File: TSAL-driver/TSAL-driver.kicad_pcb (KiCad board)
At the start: 2 copper layers, 28 parts, among them J1 OUT+, J2 OUT-, J3 IN+, J4 IN-, Q1 Q_PMOS_DGS, Q2 Q_NMOS_DGS, Q3 Q_NMOS_DGS, Q4 Q_NMOS_DGS, U1 LM556

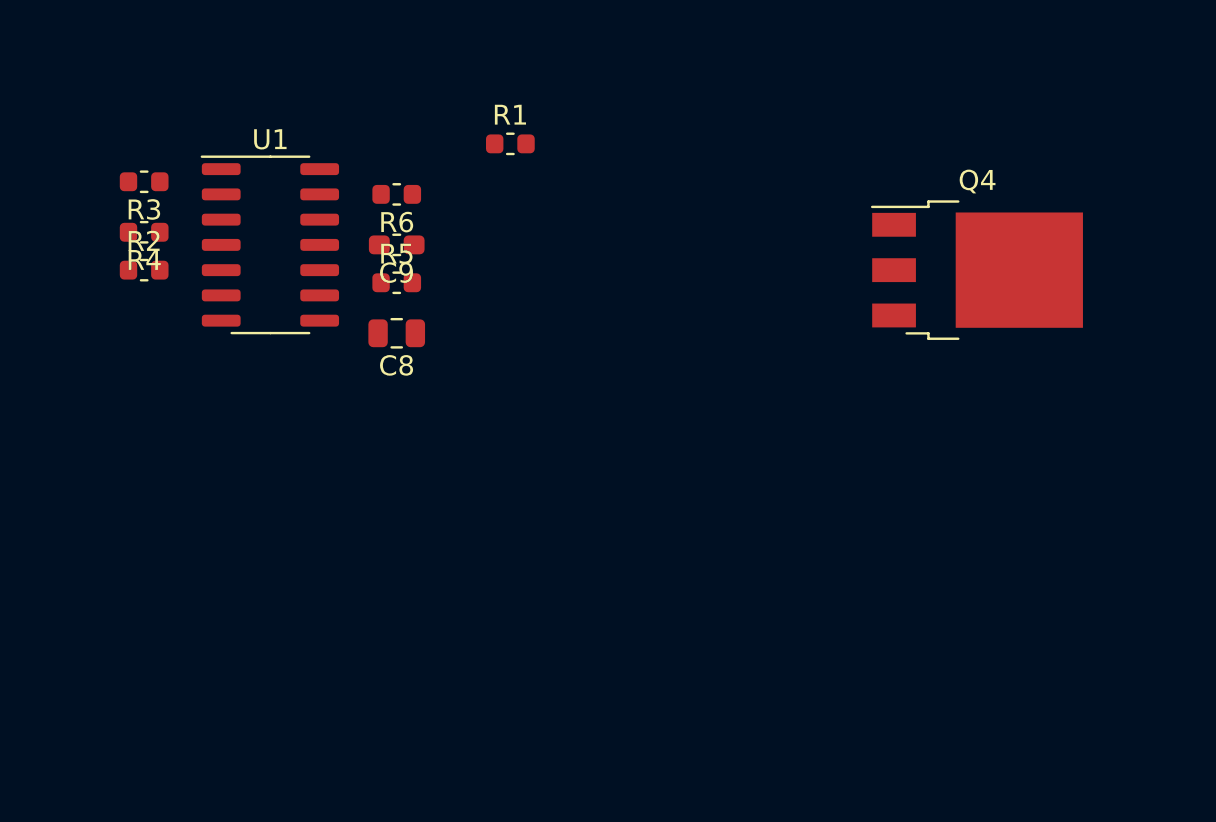
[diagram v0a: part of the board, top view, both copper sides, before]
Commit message: Started laying out TSAL-driver
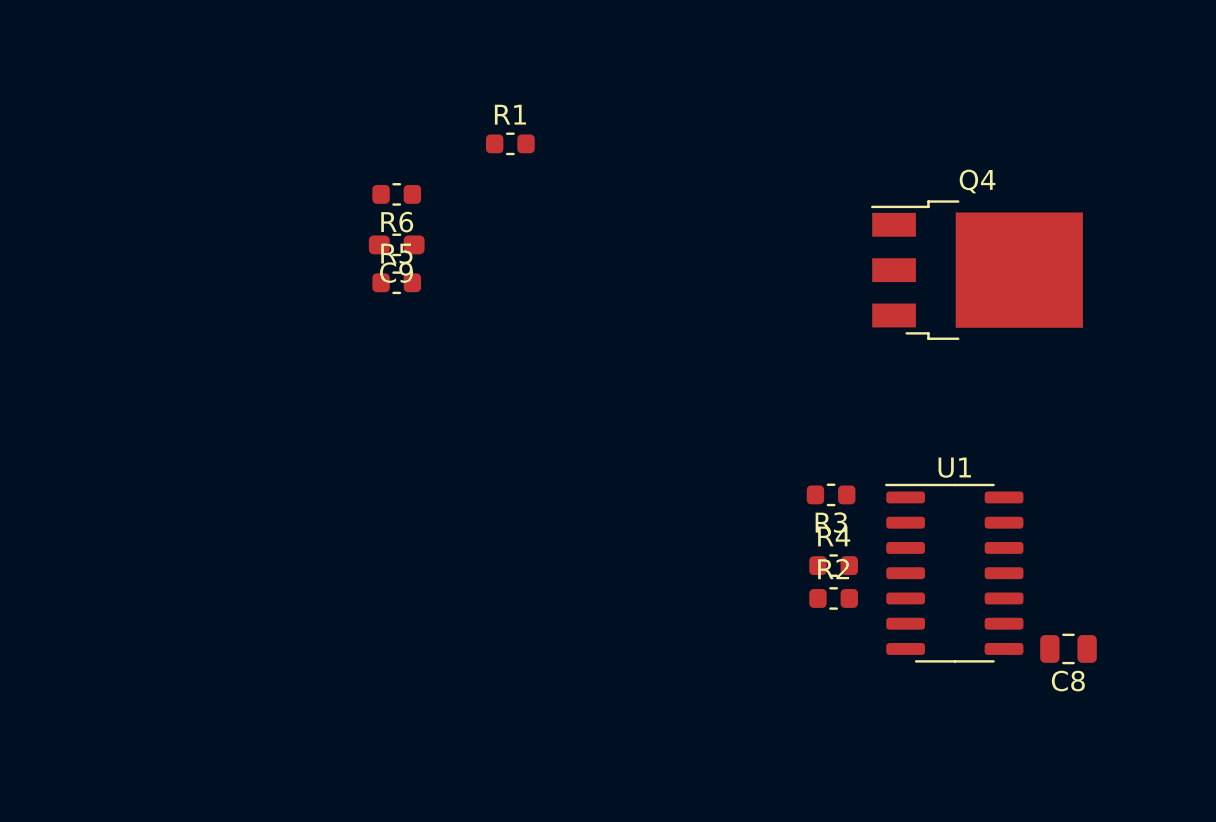
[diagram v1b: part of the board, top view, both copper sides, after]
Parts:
- moved R4 38.5 mm to (139.4, 111.4), turned to 0 degrees
- moved R2 38.4 mm to (139.4, 113.0)
- moved U1 38.2 mm to (145.5, 111.8)
- moved R3 38.0 mm to (139.3, 107.8)
- moved C8 37.3 mm to (151.3, 115.6)
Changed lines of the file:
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@@
-(kicad_pcb (version 20171130) (host pcbnew 5.1.4-e60b266~84~ubuntu16.04.1)
+(kicad_pcb (version 20171130) (host pcbnew "(5.1.2)-2")
   (general
     (thickness 1.6)
@@
     (solder_mask_min_width 0.25)
     (aux_axis_origin 0 0)
-    (visible_elements FFFFFF7F)
+    (visible_elements 7FFFFFFF)
     (pcbplotparams
       (layerselection 0x010fc_ffffffff)
@@
   )
   (module Capacitor_SMD:C_0805_2012Metric (layer F.Cu)
-    (at 117.475 99.695 180)
+    (at 151.257 115.57 180)
     (descr "Capacitor SMD 0805 (2012 Metric), square (rectangular) end terminal, IPC_7351 nominal, (Body size source: https://docs.google.com/spreadsheets/d/1BsfQQcO9C6DZCsRaXUlFlo91Tg2WpOkGARC1WS5S8t0/edit?usp=sharing), generated with kicad-footprint-generator")
     (tags capacitor)
@@
   )
   (module Resistor_SMD:R_0603_1608Metric (layer F.Cu)
-    (at 104.775 96.52)
+    (at 139.446 113.03)
     (descr "Resistor SMD 0603 (1608 Metric), square (rectangular) end terminal, IPC_7351 nominal, (Body size source: http://www.tortai-tech.com/upload/download/2011102023233369053.pdf), generated with kicad-footprint-generator")
     (tags resistor)
@@
   )
   (module Resistor_SMD:R_0603_1608Metric (layer F.Cu)
-    (at 104.775 92.075 180)
+    (at 139.319 107.823 180)
     (descr "Resistor SMD 0603 (1608 Metric), square (rectangular) end terminal, IPC_7351 nominal, (Body size source: http://www.tortai-tech.com/upload/download/2011102023233369053.pdf), generated with kicad-footprint-generator")
     (tags resistor)
@@
   )
   (module Resistor_SMD:R_0603_1608Metric (layer F.Cu)
-    (at 104.775 94.615 180)
+    (at 139.446 111.379)
     (descr "Resistor SMD 0603 (1608 Metric), square (rectangular) end terminal, IPC_7351 nominal, (Body size source: http://www.tortai-tech.com/upload/download/2011102023233369053.pdf), generated with kicad-footprint-generator")
     (tags resistor)
@@
       (effects (font (size 0.4 0.4) (thickness 0.06)))
     )
-    (pad 1 smd roundrect (at -0.7875 0 180) (size 0.875 0.95) (layers F.Cu F.Paste F.Mask) (roundrect_rratio 0.25)
+    (pad 1 smd roundrect (at -0.7875 0) (size 0.875 0.95) (layers F.Cu F.Paste F.Mask) (roundrect_rratio 0.25)
       (net 1 +12V))
-    (pad 2 smd roundrect (at 0.7875 0 180) (size 0.875 0.95) (layers F.Cu F.Paste F.Mask) (roundrect_rratio 0.25)
+    (pad 2 smd roundrect (at 0.7875 0) (size 0.875 0.95) (layers F.Cu F.Paste F.Mask) (roundrect_rratio 0.25)
       (net 3 "Net-(C2-Pad2)"))
     (model ${KISYS3DMOD}/Resistor_SMD.3dshapes/R_0603_1608Metric.wrl
@@
   )
   (module Package_SO:SOIC-14_3.9x8.7mm_P1.27mm (layer F.Cu)
-    (at 111.125 95.25)
+    (at 145.542 111.76)
     (descr "SOIC, 14 Pin (JEDEC MS-012AB, https://www.analog.com/media/en/package-pcb-resources/package/pkg_pdf/soic_narrow-r/r_14.pdf), generated with kicad-footprint-generator ipc_gullwing_generator.py")
     (tags "SOIC SO")

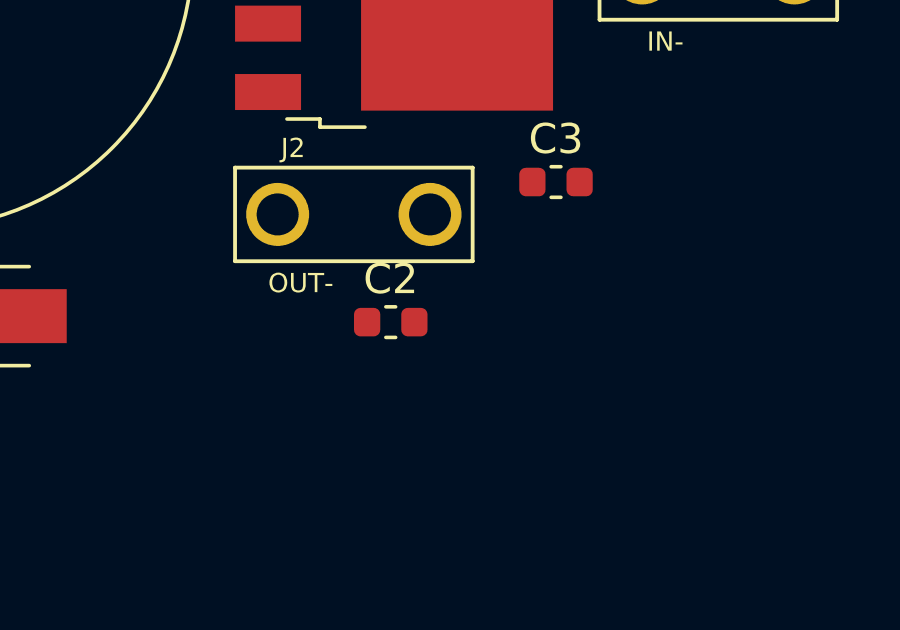
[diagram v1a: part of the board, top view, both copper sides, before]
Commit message: Moved capictor
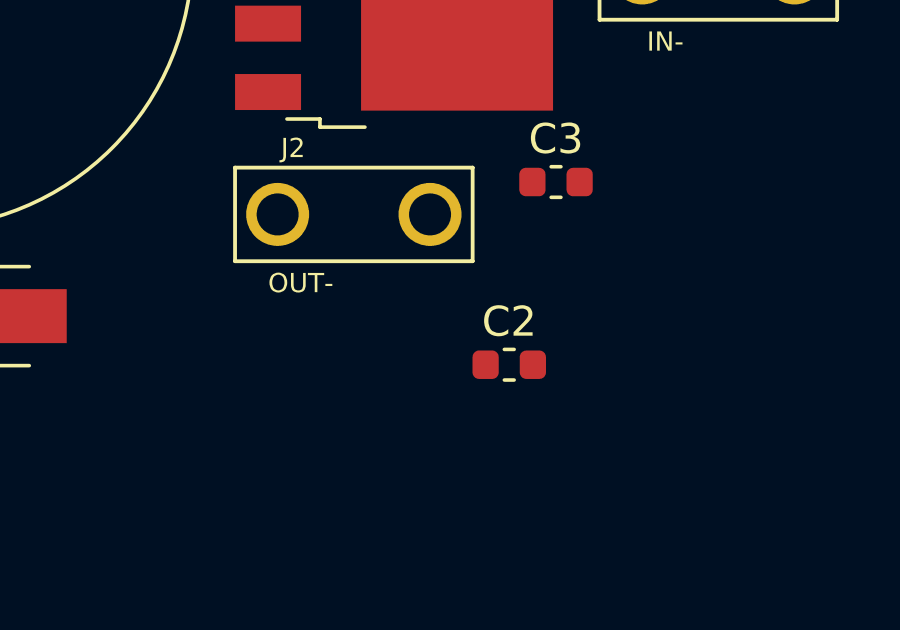
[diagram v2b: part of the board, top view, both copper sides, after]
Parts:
- moved C2 4.20 mm to (145.4, 74.3)
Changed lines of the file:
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@@
-(kicad_pcb (version 20171130) (host pcbnew "(5.1.2)-2")
+(kicad_pcb (version 20171130) (host pcbnew "(5.0.1)-3")
   (general
     (thickness 1.6)
@@
     (zone_45_only no)
     (trace_min 0.2)
+    (segment_width 0.2)
+    (edge_width 0.05)
     (via_size 0.8)
     (via_drill 0.4)
@@
     (uvia_min_size 0.2)
     (uvia_min_drill 0.1)
-    (edge_width 0.05)
-    (segment_width 0.2)
     (pcb_text_width 0.3)
     (pcb_text_size 1.5 1.5)
@@
   )
   (module Capacitor_SMD:C_0603_1608Metric (layer F.Cu)
-    (at 141.465001 72.875001)
+    (at 145.415 74.295)
     (descr "Capacitor SMD 0603 (1608 Metric), square (rectangular) end terminal, IPC_7351 nominal, (Body size source: http://www.tortai-tech.com/upload/download/2011102023233369053.pdf), generated with kicad-footprint-generator")
     (tags capacitor)

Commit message: Organized TSAL-Driver board
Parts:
- moved R7 73.3 mm to (133.0, 115.0)
- moved J1 67.9 mm to (134.0, 93.5), turned to 270 degrees
- moved Q1 67.5 mm to (123.1, 115.0), turned to 180 degrees
- moved C5 65.7 mm to (158.2, 104.5), turned to 180 degrees
- moved J3 64.8 mm to (140.0, 94.0), turned to 270 degrees
- moved C7 58.3 mm to (107.0, 117.0), turned to 90 degrees
- moved C4 57.2 mm to (153.5, 104.5), turned to 180 degrees
- moved D1 56.7 mm to (156.0, 116.0)
- moved Q3 47.9 mm to (123.0, 99.0), turned to 180 degrees
- moved Q2 47.8 mm to (123.0, 107.0), turned to 180 degrees
- moved D2 47.8 mm to (156.0, 111.0), turned to 180 degrees
- moved C3 46.8 mm to (147.8, 115.0)
- moved C1 38.3 mm to (161.0, 93.0), turned to 180 degrees
- moved C2 36.8 mm to (147.8, 111.0), turned to 180 degrees
- moved C6 34.7 mm to (107.0, 95.0), turned to 90 degrees
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
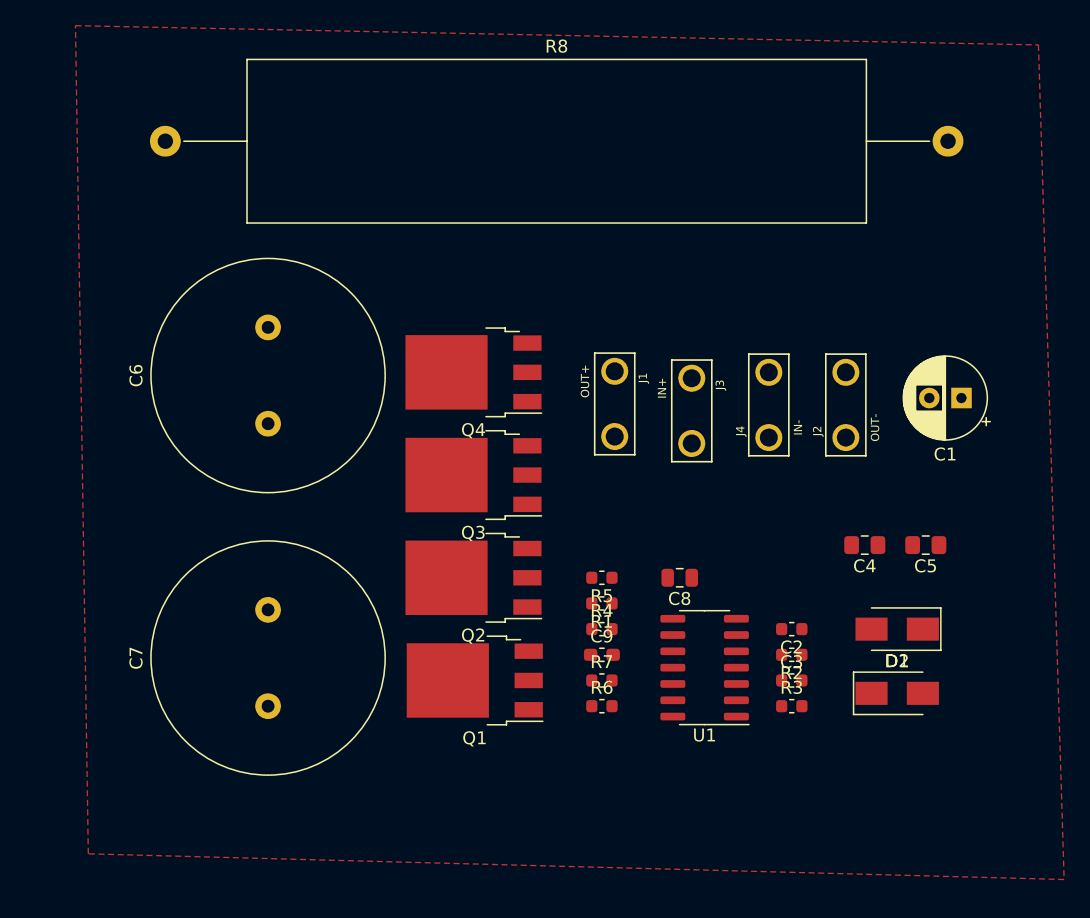
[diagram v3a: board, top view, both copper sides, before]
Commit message: Inputs and Outputs are on Opposite Sides
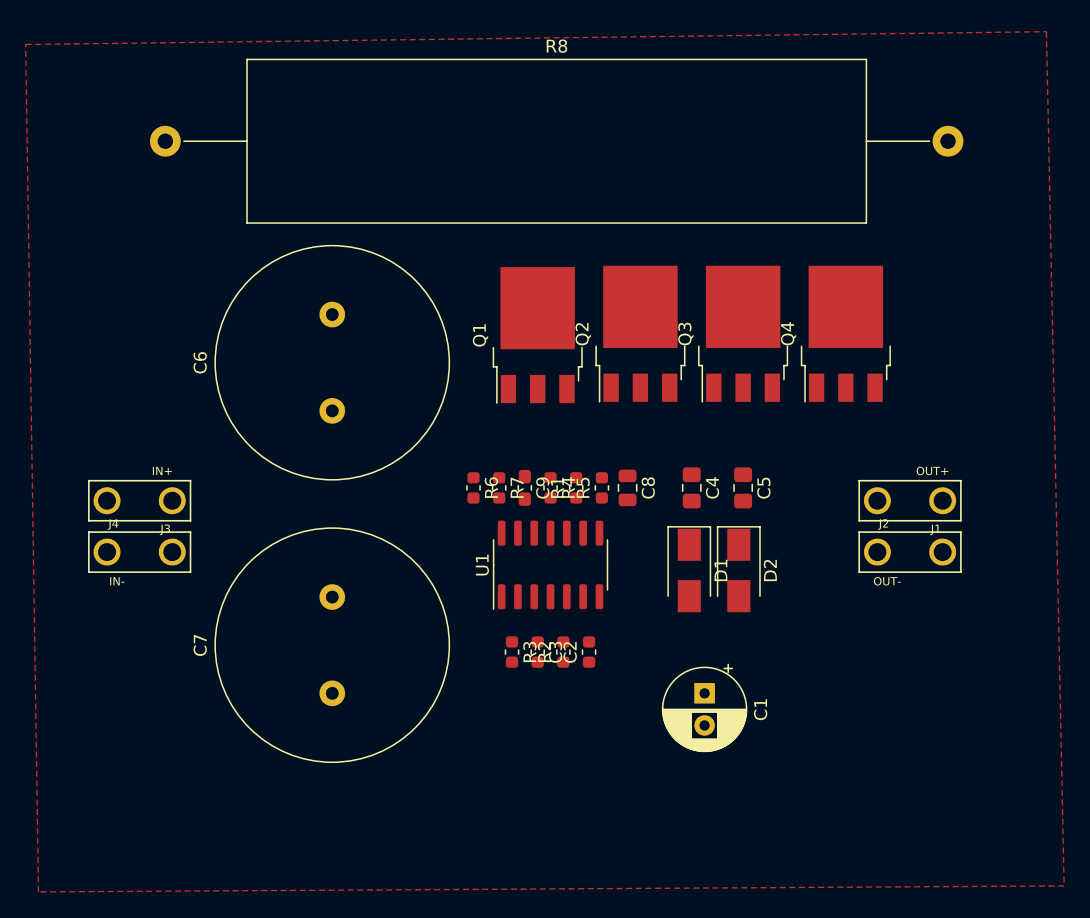
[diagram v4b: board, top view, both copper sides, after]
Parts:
- moved J4 50.3 mm to (97.0, 105.0), turned to 0 degrees
- moved J3 43.6 mm to (97.0, 101.0), turned to 180 degrees
- moved C1 30.5 mm to (141.0, 116.0), turned to 270 degrees
- moved Q4 29.2 mm to (152.0, 88.0), turned to 90 degrees
- moved Q1 27.3 mm to (128.0, 88.1), turned to 90 degrees
- moved J1 24.2 mm to (157.0, 101.0), turned to 180 degrees
- moved Q3 23.7 mm to (144.0, 88.0), turned to 90 degrees
- moved Q2 23.0 mm to (136.0, 88.0), turned to 90 degrees
- moved R3 22.2 mm to (126.0, 112.8), turned to 270 degrees
- moved C3 19.9 mm to (128.0, 112.8), turned to 270 degrees
- moved R6 19.7 mm to (123.0, 100.0), turned to 270 degrees
- moved D1 18.8 mm to (139.8, 106.4), turned to 270 degrees
- moved R2 17.8 mm to (130.0, 112.8), turned to 90 degrees
- moved R7 17.0 mm to (125.0, 100.0), turned to 270 degrees
- moved C2 15.9 mm to (132.0, 112.8), turned to 90 degrees
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
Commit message: Finished TSAL-driver
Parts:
- removed C5: 10u, Capacitor_SMD:C_0805_2012Metric_Pad1.15x1.40mm_HandSolder
- removed C6, C7: 4700uF, Capacitor_THT:C_Radial_D18.0mm_H35.5mm_P7.50mm
- removed C8: 10u, Capacitor_SMD:C_0805_2012Metric
- removed C9: 0.01, Capacitor_SMD:C_0603_1608Metric_Pad1.05x0.95mm_HandSolder
- removed D1, D2: 1N4001, Diode_SMD:D_SMA
- removed Q1: Q_PMOS_DGS, Package_TO_SOT_SMD:TO-252-3_TabPin2
- removed Q2, Q3, Q4: Q_NMOS_DGS, Package_TO_SOT_SMD:TO-252-3_TabPin2
- removed R1, R3: 10k, Resistor_SMD:R_0603_1608Metric
- removed R2, R4, R5: 100, Resistor_SMD:R_0603_1608Metric
- removed R6: 4.7k, Resistor_SMD:R_0603_1608Metric
- removed R7: 39k, Resistor_SMD:R_0603_1608Metric
- removed R8: 10, Resistor_THT:R_Axial_Power_L48.0mm_W12.5mm_P60.96mm
- added G***: LOGO, AERO-footprints:AERO_Logo_15x6mm, F.Cu at (130.8, 74.9)
- added U2: ATtiny25-20SSU, Package_SO:SOIC-8_3.9x4.9mm_P1.27mm, F.Cu at (134.0, 87.0)
- added U3: LDB-350L, AERO-footprints:DIP1549W45P254L3404H940Q24, B.Cu at (133.9, 85.9)
- C1: value 100u -> 0.1uF; footprint Capacitor_THT:CP_Radial_D6.3mm_P2.50mm -> Capacitor_SMD:C_0603_1608Metric
- C2: value 10n -> 10uF
- C3: value 0.01u -> 10uF
- C4: value 10u -> 10uF; footprint Capacitor_SMD:C_0805_2012Metric_Pad1.15x1.40mm_HandSolder -> Capacitor_SMD:C_0603_1608Metric
- J1: value OUT+ -> LED+; footprint 1217861-1:TE_1217861-1 -> AERO-footprints:TE_1217861-1
- J2: value OUT- -> LED-; footprint 1217861-1:TE_1217861-1 -> AERO-footprints:TE_1217861-1
- J3: value IN+ -> 12V; footprint 1217861-1:TE_1217861-1 -> AERO-footprints:TE_1217861-1
- J4: value IN- -> GND; footprint 1217861-1:TE_1217861-1 -> AERO-footprints:TE_1217861-1
- U1: value LM556 -> AZ1117-5.0; footprint Package_SO:SOIC-14_3.9x8.7mm_P1.27mm -> Package_TO_SOT_SMD:SOT-223-3_TabPin2
- moved J2 51.4 mm to (127.6, 62.9), turned to 90 degrees
- moved J3 43.5 mm to (139.7, 109.2), turned to 90 degrees
- moved J1 41.9 mm to (139.7, 62.9), turned to 90 degrees
- moved C1 33.2 mm to (135.9, 83.2), turned to 180 degrees
- moved J4 30.9 mm to (127.6, 109.2), turned to 90 degrees
- moved C3 17.6 mm to (129.5, 95.2)
- moved U1 11.4 mm to (135.3, 96.5), turned to 0 degrees
- moved C2 11.2 mm to (132.7, 101.6), turned to 180 degrees
- moved C4 2.24 mm to (138.4, 101.6), turned to 0 degrees
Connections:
- C1 pad 1: +12V -> +5V
- C2 pad 2: Net-(C2-Pad2) -> +12V
- C3 pad 2: Net-(C3-Pad2) -> +5V
- C4 pad 1: Net-(C4-Pad1) -> GND
- C4 pad 2: Net-(C4-Pad2) -> +12V
- J1 pad 1: Net-(J1-Pad1) -> +24V
- J2 pad 1: /LED- -> GND
- U1 pad 1: Net-(R3-Pad1) -> GND
- U1 pad 2: Net-(C2-Pad2) -> +5V
- U1 pad 3: Net-(C3-Pad2) -> +12V
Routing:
- net +12V: track 0.00 -> 29.9 mm
- net +5V: track 0.00 -> 25.8 mm
- net +24V: track 0.00 -> 14.9 mm
- net /PWM_DIM: track 0.00 -> 8.25 mm
- added copper zone on B.Cu, net GND
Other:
- board outline added: 20.3 x 56.5 mm
- net class 5V added: clearance 0.381, trace_width 0.635, via_dia 0.8, via_drill 0.4
- net class Default: clearance 0.2 -> 0.381; trace_width 0.25 -> 0.381
- net class Power added: clearance 0.381, trace_width 1.27, via_dia 0.8, via_drill 0.4
- rule trace_clearance: 0.2 -> 0.381
- board text added: "TSAL-driver 19.281"
- board text added: "W. Hillier D. Morton C. Fung"

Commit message: Cleaned up board, added 3D
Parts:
- J1, J2, J3, J4: moved to B.Cu
- turned J1 to 270 degrees
- turned J2 to 270 degrees
- turned J3 to 270 degrees
- turned J4 to 270 degrees
